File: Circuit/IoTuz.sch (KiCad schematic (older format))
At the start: 29 parts, among them P1 Alligator Connector, P2 BATTERY, P3 USB_5PIN_SHELL, P4 LED_1, P5 LED_2, P6 CONN_01X20, P7 CONN_01X20, Q1 S8050, Q2 S8050, Q3 FDN340P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

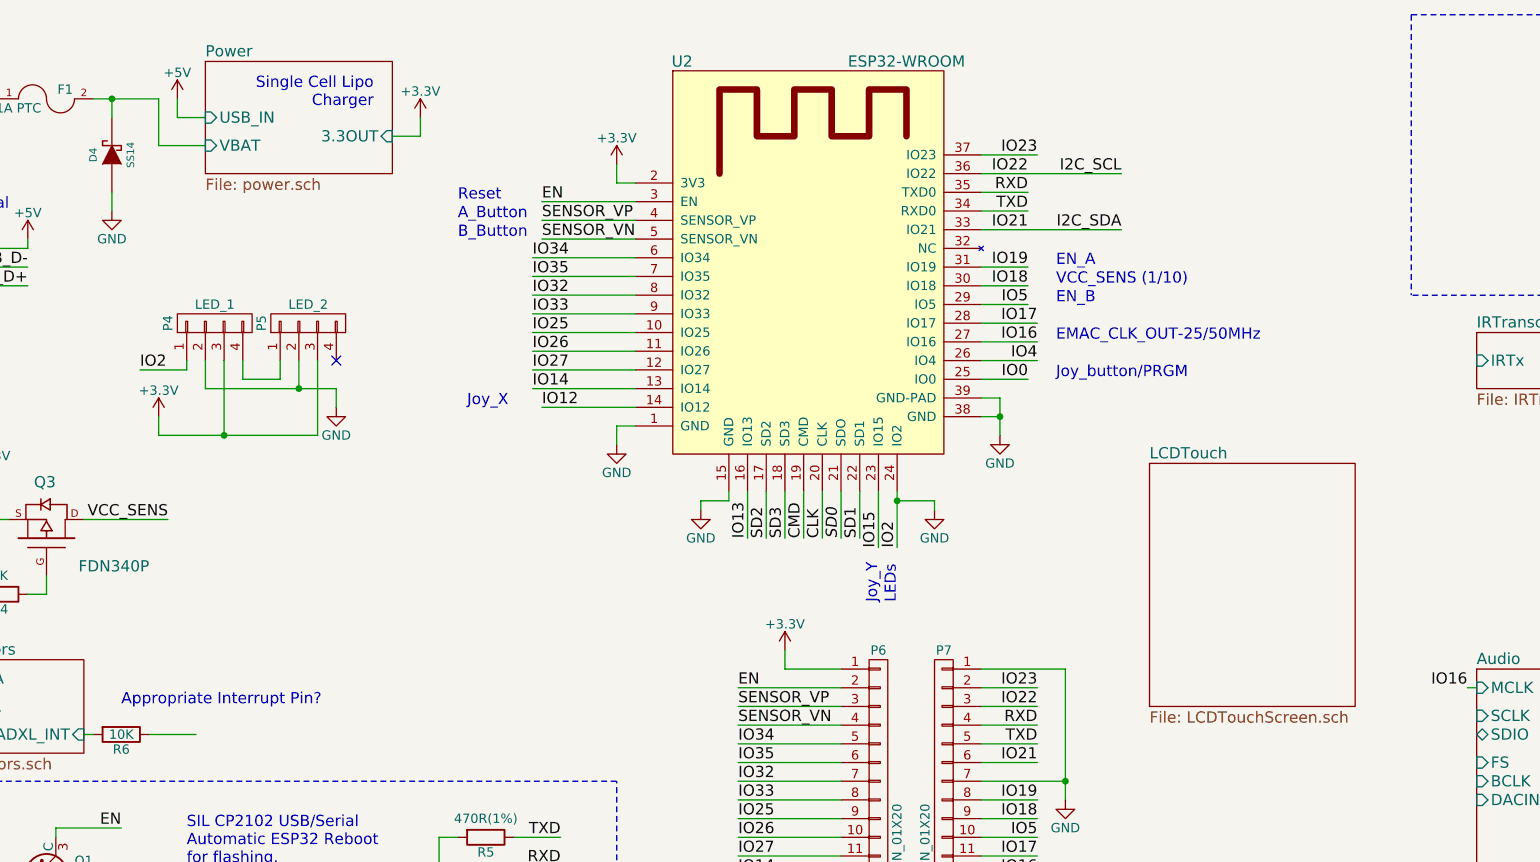
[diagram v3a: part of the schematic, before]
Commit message: Pins to LCD sheet.
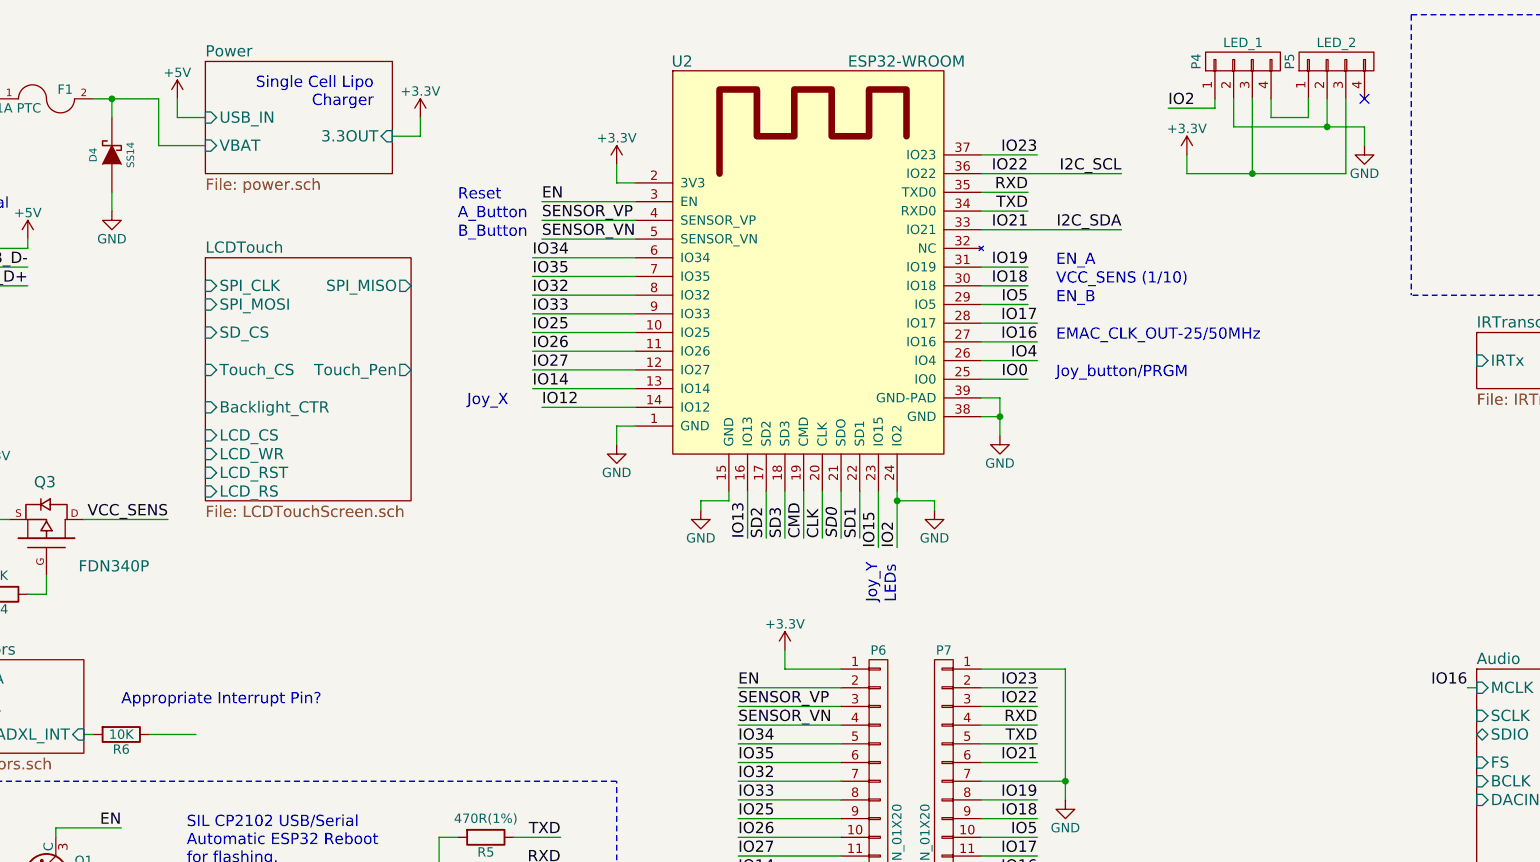
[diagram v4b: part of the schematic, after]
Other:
- moved on the sheet: P4, P5
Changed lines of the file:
@@
 L CONN_01X04 P4
 U 1 1 580D7B68
-P 2550 2050
-F 0 "P4" H 2550 2300 50  0000 C CNN
-F 1 "LED_1" V 2650 2050 50  0000 C CNN
-F 2 "libs:LED_8MM_APA-106" H 2550 2050 50  0001 C CNN
-F 3 "" H 2550 2050 50  0000 C CNN
-	1    2550 2050
+P 8050 650
+F 0 "P4" H 8050 900 50  0000 C CNN
+F 1 "LED_1" V 8150 650 50  0000 C CNN
+F 2 "libs:LED_8MM_APA-106" H 8050 650 50  0001 C CNN
+F 3 "" H 8050 650 50  0000 C CNN
+	1    8050 650
 	0    -1   -1   0
 $EndComp
@@
 L CONN_01X04 P5
 U 1 1 580D86C3
-P 3050 2050
-F 0 "P5" H 3050 2300 50  0000 C CNN
-F 1 "LED_2" V 3150 2050 50  0000 C CNN
-F 2 "libs:LED_8MM_APA-106" H 3050 2050 50  0001 C CNN
-F 3 "" H 3050 2050 50  0000 C CNN
-	1    3050 2050
+P 8550 650
+F 0 "P5" H 8550 900 50  0000 C CNN
+F 1 "LED_2" V 8650 650 50  0000 C CNN
+F 2 "libs:LED_8MM_APA-106" H 8550 650 50  0001 C CNN
+F 3 "" H 8550 650 50  0000 C CNN
+	1    8550 650
 	0    -1   -1   0
 $EndComp
-Text Label 2150 2300 0    60   ~ 0
+Text Label 7650 900  0    60   ~ 0
 IO2
-NoConn ~ 3200 2250
+NoConn ~ 8700 850
 $Comp
 L +3.3V #PWR018
 U 1 1 580DAAD9
-P 2250 2550
-F 0 "#PWR018" H 2250 2400 50  0001 C CNN
-F 1 "+3.3V" H 2250 2690 50  0000 C CNN
-F 2 "" H 2250 2550 50  0000 C CNN
-F 3 "" H 2250 2550 50  0000 C CNN
-	1    2250 2550
+P 7750 1150
+F 0 "#PWR018" H 7750 1000 50  0001 C CNN
+F 1 "+3.3V" H 7750 1290 50  0000 C CNN
+F 2 "" H 7750 1150 50  0000 C CNN
+F 3 "" H 7750 1150 50  0000 C CNN
+	1    7750 1150
 	1    0    0    -1
 $EndComp
@@
 L GND #PWR019
 U 1 1 580DAB83
-P 3200 2500
-F 0 "#PWR019" H 3200 2250 50  0001 C CNN
-F 1 "GND" H 3200 2350 50  0000 C CNN
-F 2 "" H 3200 2500 50  0000 C CNN
-F 3 "" H 3200 2500 50  0000 C CNN
-	1    3200 2500
+P 8700 1100
+F 0 "#PWR019" H 8700 850 50  0001 C CNN
+F 1 "GND" H 8700 950 50  0000 C CNN
+F 2 "" H 8700 1100 50  0000 C CNN
+F 3 "" H 8700 1100 50  0000 C CNN
+	1    8700 1100
 	1    0    0    -1
 $EndComp
@@
 $EndSheet
 $Sheet
-S 7550 2800 1100 1300
+S 2500 1700 1100 1300
 U 5811E13F
 F0 "LCDTouch" 60
 F1 "LCDTouchScreen.sch" 60
+F2 "SPI_MISO" O R 3600 1850 60
+F3 "SPI_CLK" I L 2500 1850 60
+F4 "SPI_MOSI" I L 2500 1950 60
+F5 "SD_CS" I L 2500 2100 60
+F6 "Touch_CS" I L 2500 2300 60
+F7 "Touch_Pen" O R 3600 2300 60
+F8 "Backlight_CTR" I L 2500 2500 60
+F9 "LCD_CS" I L 2500 2650 60
+F10 "LCD_WR" I L 2500 2750 60
+F11 "LCD_RST" I L 2500 2850 60
+F12 "LCD_RS" I L 2500 2950 60
 $EndSheet
 $Sheet
@@
 	5150 3000 5150 3050
 Wire Wire Line
-	2700 2250 2700 2350
-Wire Wire Line
-	2700 2350 2900 2350
-Wire Wire Line
-	2900 2350 2900 2250
-Wire Wire Line
-	2400 2250 2400 2300
-Wire Wire Line
-	2400 2300 2150 2300
-Wire Wire Line
-	2600 2250 2600 2650
-Wire Wire Line
-	2250 2650 3100 2650
-Wire Wire Line
-	2250 2650 2250 2550
-Wire Wire Line
-	3100 2650 3100 2250
-Connection ~ 2600 2650
-Wire Wire Line
-	2500 2250 2500 2400
-Wire Wire Line
-	2500 2400 3200 2400
-Wire Wire Line
-	3200 2400 3200 2500
-Wire Wire Line
-	3000 2250 3000 2400
-Connection ~ 3000 2400
+	8200 850  8200 950
+Wire Wire Line
+	8200 950  8400 950
+Wire Wire Line
+	8400 950  8400 850
+Wire Wire Line
+	7900 850  7900 900
+Wire Wire Line
+	7900 900  7650 900
+Wire Wire Line
+	8100 850  8100 1250
+Wire Wire Line
+	7750 1250 8600 1250
+Wire Wire Line
+	7750 1250 7750 1150
+Wire Wire Line
+	8600 1250 8600 850
+Connection ~ 8100 1250
+Wire Wire Line
+	8000 850  8000 1000
+Wire Wire Line
+	8000 1000 8700 1000
+Wire Wire Line
+	8700 1000 8700 1100
+Wire Wire Line
+	8500 850  8500 1000
+Connection ~ 8500 1000
 Wire Wire Line
 	1850 3100 2300 3100

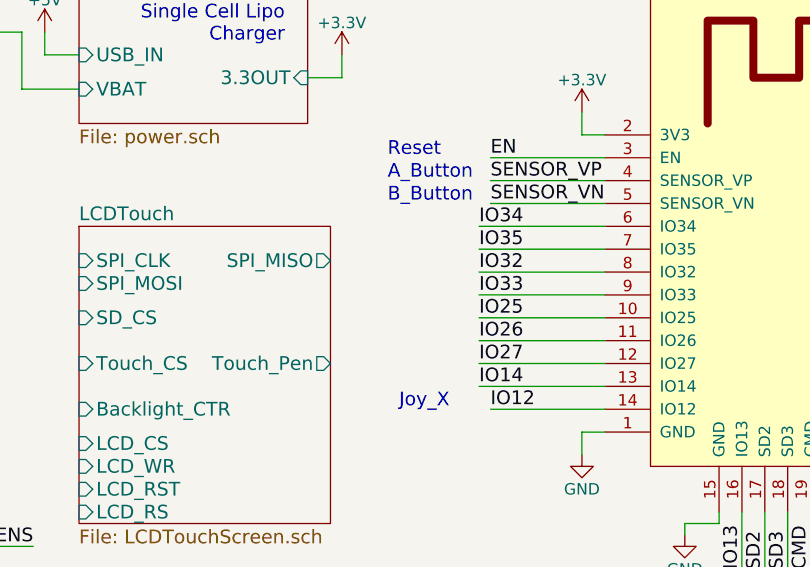
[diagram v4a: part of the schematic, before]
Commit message: Adding some component information, connecting audio.
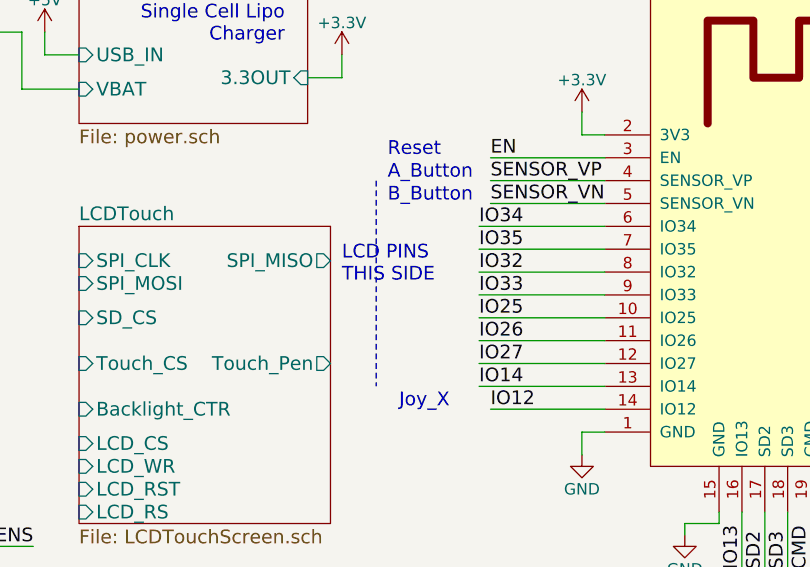
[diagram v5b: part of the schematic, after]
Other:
- note added: "LCD PINS\nTHIS SIDE"
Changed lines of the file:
@@
 Wire Wire Line
 	5750 6100 5750 6150
+Wire Notes Line
+	3800 1500 3800 2400
+Text Notes 3650 1950 0    60   ~ 0
+LCD PINS\nTHIS SIDE
 $EndSCHEMATC

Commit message: More component information.
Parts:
- Q1, Q2: Digikey PN (none) -> MMSS8050-H-TPMSCT-ND; Link (none) -> http://www.digikey.com.au/product-detail/en/micro-commercia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; Manufactuer PN (none) -> MMSS8050-H-TP; Unit Cost (none) -> 0.20
- R1, R2: Digikey PN (none) -> 311-12.0KHRCT-ND; Link (none) -> http://www.digikey.com.au/product-detail/en/yageo/RC0603FR-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; Manufacturer PN (none) -> RC0603FR-0712KL; Unit Cost (none) -> 0.10
- U1: Digikey PN (none) -> 336-1160-1-ND; Link (none) -> http://www.digikey.com.au/product-detail/en/silicon-labs/CP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; Manufacturer PN (none) -> CP2102-GMR; Unit Cost (none) -> 2.88
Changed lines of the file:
@@
 F 2 "Housings_DFN_QFN:QFN-28-1EP_5x5mm_Pitch0.5mm" H 3800 6200 60  0001 C CNN
 F 3 "" H 3800 6200 60  0000 C CNN
+F 4 "336-1160-1-ND" H 3800 6200 60  0001 C CNN "Digikey PN"
+F 5 "http://www.digikey.com.au/product-detail/en/silicon-labs/CP2102-GMR/336-1160-1-ND/3672615" H 3800 6200 60  0001 C CNN "Link"
+F 6 "CP2102-GMR" H 3800 6200 60  0001 C CNN "Manufacturer PN"
+F 7 "2.88" H 3800 6200 60  0001 C CNN "Unit Cost"
 	1    3800 6200
 	1    0    0    -1
@@
 F 2 "Resistors_SMD:R_0603_HandSoldering" V 1030 5000 50  0001 C CNN
 F 3 "" H 1100 5000 50  0000 C CNN
+F 4 "311-12.0KHRCT-ND" V 1100 5000 60  0001 C CNN "Digikey PN"
+F 5 "http://www.digikey.com.au/product-detail/en/yageo/RC0603FR-0712KL/311-12.0KHRCT-ND/729860" V 1100 5000 60  0001 C CNN "Link"
+F 6 "RC0603FR-0712KL" V 1100 5000 60  0001 C CNN "Manufacturer PN"
+F 7 "0.10" V 1100 5000 60  0001 C CNN "Unit Cost"
 	1    1100 5000
 	0    1    1    0
@@
 F 2 "Resistors_SMD:R_0603_HandSoldering" V 1030 5650 50  0001 C CNN
 F 3 "" H 1100 5650 50  0000 C CNN
+F 4 "311-12.0KHRCT-ND" V 1100 5000 60  0001 C CNN "Digikey PN"
+F 5 "http://www.digikey.com.au/product-detail/en/yageo/RC0603FR-0712KL/311-12.0KHRCT-ND/729860" V 1100 5000 60  0001 C CNN "Link"
+F 6 "RC0603FR-0712KL" V 1100 5000 60  0001 C CNN "Manufacturer PN"
+F 7 "0.10" V 1100 5000 60  0001 C CNN "Unit Cost"
 	1    1100 5650
 	0    1    1    0
@@
 F 2 "TO_SOT_Packages_SMD:SOT-23_Handsoldering" H 1800 4925 50  0000 L CIN
 F 3 "" H 1600 5000 50  0000 L CNN
+F 4 "MMSS8050-H-TPMSCT-ND" H 1600 5000 60  0001 C CNN "Digikey PN"
+F 5 "http://www.digikey.com.au/product-detail/en/micro-commercial-co/MMSS8050-H-TP/MMSS8050-H-TPMSCT-ND/2825945" H 1600 5000 60  0001 C CNN "Link"
+F 6 "MMSS8050-H-TP" H 1600 5000 60  0001 C CNN "Manufactuer PN"
+F 7 "0.20" H 1600 5000 60  0001 C CNN "Unit Cost"
 	1    1600 5000
 	1    0    0    -1
@@
 F 2 "TO_SOT_Packages_SMD:SOT-23_Handsoldering" H 1800 5575 50  0000 L CIN
 F 3 "" H 1600 5650 50  0000 L CNN
+F 4 "MMSS8050-H-TPMSCT-ND" H 1600 5000 60  0001 C CNN "Digikey PN"
+F 5 "http://www.digikey.com.au/product-detail/en/micro-commercial-co/MMSS8050-H-TP/MMSS8050-H-TPMSCT-ND/2825945" H 1600 5000 60  0001 C CNN "Link"
+F 6 "MMSS8050-H-TP" H 1600 5000 60  0001 C CNN "Manufactuer PN"
+F 7 "0.20" H 1600 5000 60  0001 C CNN "Unit Cost"
 	1    1600 5650
 	1    0    0    1

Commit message: More component info & rework footprint for the USB connector.
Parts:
- P3: footprint freetronics_footprints:USB-MICRO-5pin_PTHMOUNT -> libs:USB-MICRO-5pin_PTHMOUNT-Amphenol.10118194-0001LF; Digikey PN (none) -> 609-4618-1-ND; Link (none) -> http://www.digikey.com.au/product-detail/en/amphenol-fci/10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; Manufacturer PN (none) -> 10118194-0001LF; Unit Cost (none) -> 0.46
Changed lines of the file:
@@
 F 0 "P3" H 875 2050 60  0000 C CNN
 F 1 "USB_5PIN_SHELL" H 800 1450 60  0001 L CNN
-F 2 "freetronics_footprints:USB-MICRO-5pin_PTHMOUNT" H 800 1400 31  0001 L CNN
+F 2 "libs:USB-MICRO-5pin_PTHMOUNT-Amphenol.10118194-0001LF" H 800 1400 31  0001 L CNN
 F 3 "" H 950 1800 60  0000 C CNN
+F 4 "609-4618-1-ND" H 950 1800 60  0001 C CNN "Digikey PN"
+F 5 "http://www.digikey.com.au/product-detail/en/amphenol-fci/10118194-0001LF/609-4618-1-ND/2785382" H 950 1800 60  0001 C CNN "Link"
+F 6 "10118194-0001LF" H 950 1800 60  0001 C CNN "Manufacturer PN"
+F 7 "0.46" H 950 1800 60  0001 C CNN "Unit Cost"
 	1    950  1800
 	1    0    0    -1

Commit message: Most power schematic component information added.
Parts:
- R13, R5: Digikey PN (none) -> 311-470HRCT-ND; Link (none) -> http://www.digikey.com.au/product-detail/en/yageo/RC0603FR-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; Manufacturer PN (none) -> RC0603FR-07470RL; Unit Cost (none) -> 0.10
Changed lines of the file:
@@
 Text Label 3950 5200 3    60   ~ 0
 RTS
-$Comp
-L R R5
-U 1 1 5807D87D
-P 4000 4800
-F 0 "R5" V 4080 4800 50  0000 C CNN
-F 1 "470R(1%)" V 3900 4800 50  0000 C CNN
-F 2 "Resistors_SMD:R_0603_HandSoldering" V 3930 4800 50  0001 C CNN
-F 3 "" H 4000 4800 50  0000 C CNN
-	1    4000 4800
-	0    1    1    0
-$EndComp
 Text Label 4400 4950 2    60   ~ 0
 RXD
@@
 F 2 "Resistors_SMD:R_0603_HandSoldering" V 10730 800 50  0001 C CNN
 F 3 "" H 10800 800 50  0000 C CNN
+F 4 "311-470HRCT-ND" V 10800 800 60  0001 C CNN "Digikey PN"
+F 5 "http://www.digikey.com.au/product-detail/en/yageo/RC0603FR-07470RL/311-470HRCT-ND/730203" V 10800 800 60  0001 C CNN "Link"
+F 6 "RC0603FR-07470RL" V 10800 800 60  0001 C CNN "Manufacturer PN"
+F 7 "0.10" V 10800 800 60  0001 C CNN "Unit Cost"
 	1    10800 800
 	0    1    1    0
@@
 Text Notes 3650 1950 0    60   ~ 0
 LCD PINS\nTHIS SIDE
+$Comp
+L R R5
+U 1 1 5820E1F5
+P 4000 4800
+F 0 "R5" V 4080 4800 50  0000 C CNN
+F 1 "470R(1%)" V 3900 4800 50  0000 C CNN
+F 2 "Resistors_SMD:R_0603_HandSoldering" V 3930 4800 50  0001 C CNN
+F 3 "" H 4000 4800 50  0000 C CNN
+F 4 "311-470HRCT-ND" V 4000 4800 60  0001 C CNN "Digikey PN"
+F 5 "http://www.digikey.com.au/product-detail/en/yageo/RC0603FR-07470RL/311-470HRCT-ND/730203" V 4000 4800 60  0001 C CNN "Link"
+F 6 "RC0603FR-07470RL" V 4000 4800 60  0001 C CNN "Manufacturer PN"
+F 7 "0.10" V 4000 4800 60  0001 C CNN "Unit Cost"
+	1    4000 4800
+	0    1    1    0
+$EndComp
 $EndSCHEMATC
